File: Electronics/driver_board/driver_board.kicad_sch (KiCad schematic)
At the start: 22 parts, among them J1 Conn_ST_STDC14, J2 Conn_01x02, Q1 IAUZ40N10S5N130, Q2 IAUZ40N10S5N130, Q3 IAUZ40N10S5N130, Q4 IAUZ40N10S5N130, U1 INA241A2xDDF, U2 STM32G491CCT6, U3 REF3433TIDBVR, U4 UCC27302ADRCR, U5 UCC27302ADRCR, U6 LMW78_12-0.5R

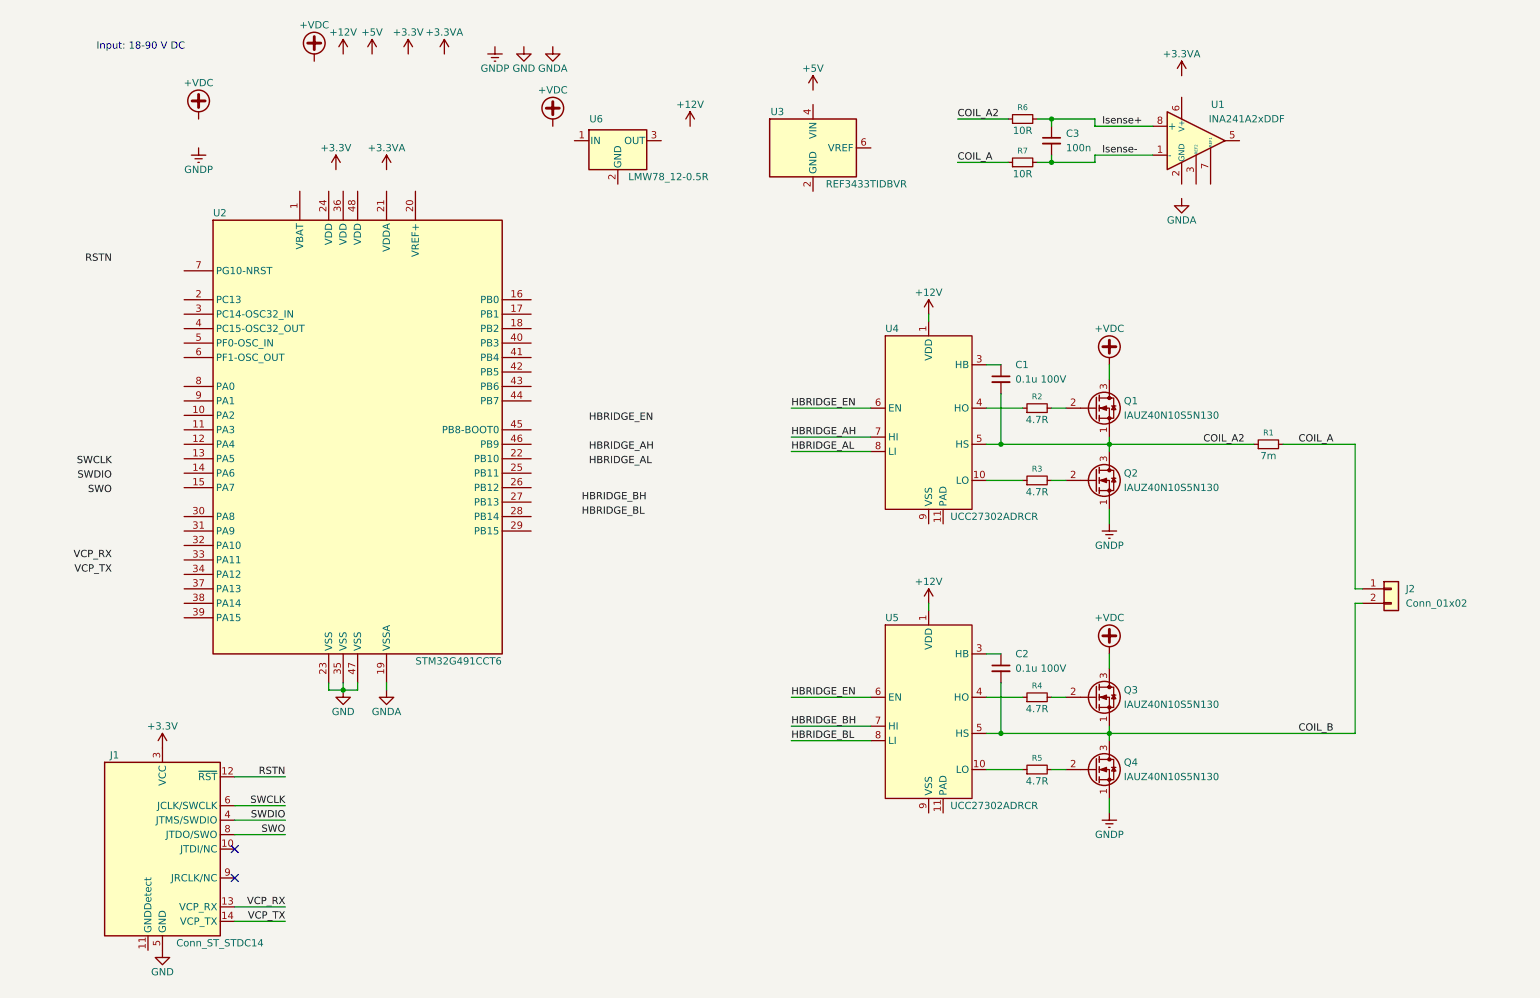
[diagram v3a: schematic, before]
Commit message: [pcb] Added more power supply parts, split power to separate sheet
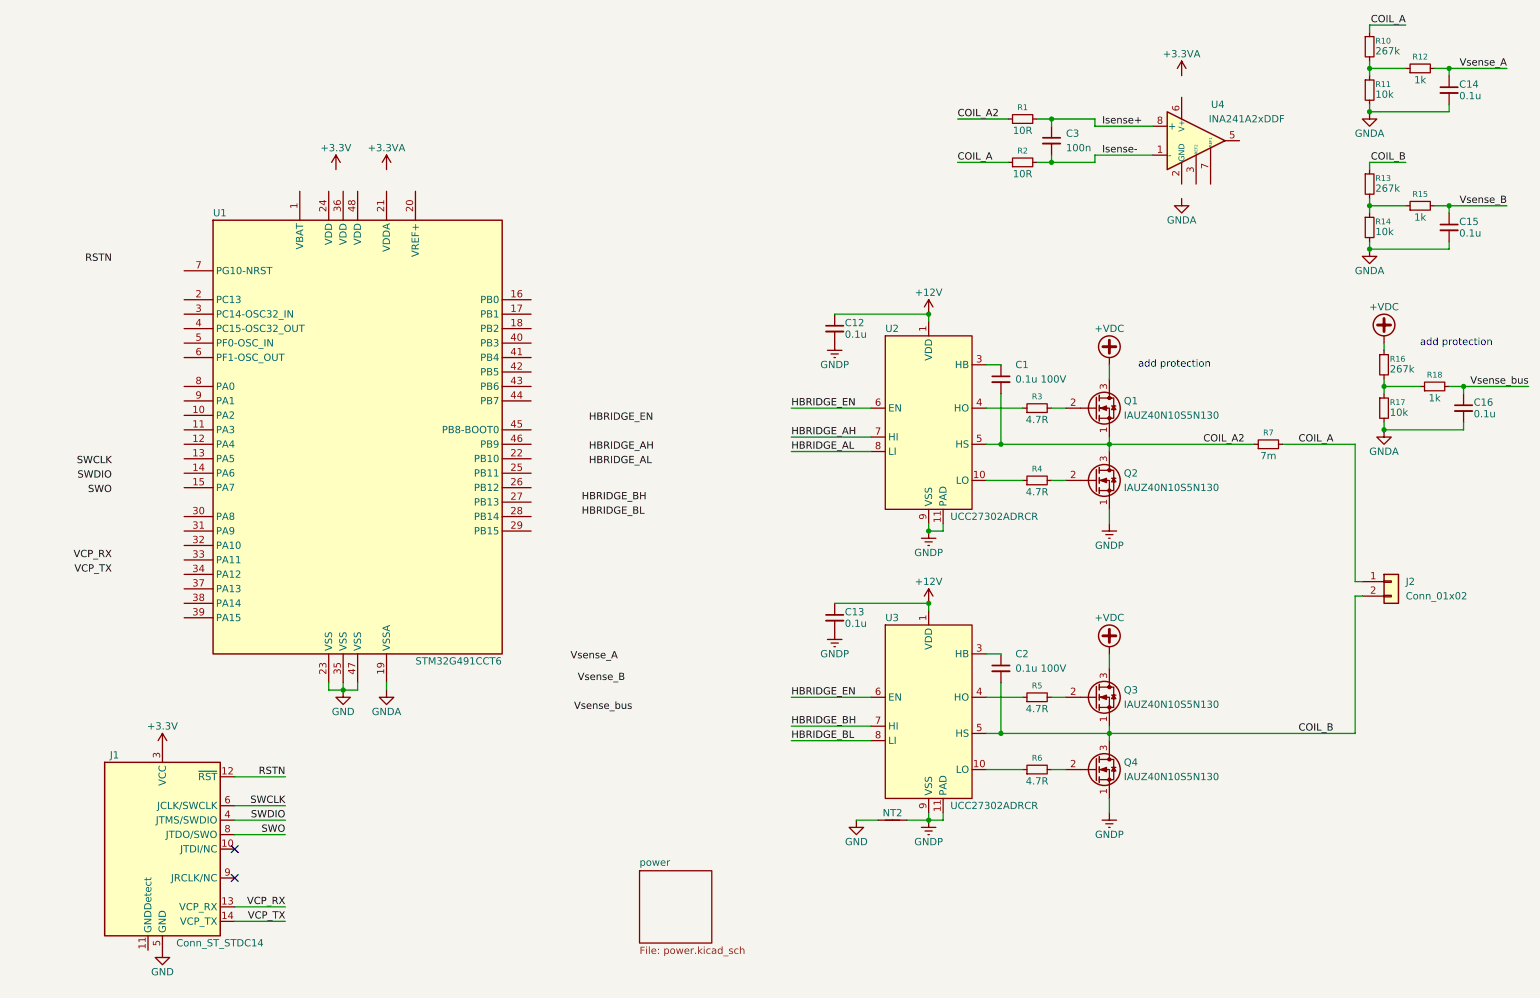
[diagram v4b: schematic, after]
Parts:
- removed U3: REF3433TIDBVR, Package_TO_SOT_SMD:SOT-23-6, symbol DWlib:REF3433TIDBVR
- removed U6: LMW78_12-0.5R, DWlib:Converter_DCDC_GAPTEC_LMW78_THT, symbol DWlib:LMW78_0.5R
- added C12, C13, C14, C15, C16: 0.1u, symbol Device:C_Small
- added NT2: NetTie_2, NetTie:NetTie-2_SMD_Pad0.5mm, symbol Device:NetTie_2
- added R10, R13, R16: 267k, symbol Device:R_Small
- added R11, R14, R17: 10k, symbol Device:R_Small
- added R12, R15, R18: 1k, symbol Device:R_Small
- renumbered R6 to R1, R7 to R2, R2 to R3, R3 to R4, R4 to R5, R5 to R6, R1 to R7, U2 to U1, U4 to U2, U5 to U3, U1 to U4
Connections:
- net +12V: now also C12.1, C13.1
- net +VDC: now also R16.1
- net COIL_A: now also R10.1
- net COIL_B: now also R13.1
- net GND: now also NT2.1
- net GNDA: now also C14.2, C15.2, C16.2, R11.2, R14.2, R17.2
- net GNDP: now also U2.11 (PAD), U2.9 (VSS), U3.11 (PAD), U3.9 (VSS), C12.2, C13.2, NT2.2
- new net: R16.2, R17.1, R18.1
- new net: R13.2, R14.1, R15.1
- new net: R10.2, R11.1, R12.1
- new net Vsense_A: C14.1, R12.2
- new net Vsense_B: C15.1, R15.2
- new net Vsense_bus: C16.1, R18.2
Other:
- added sheet power (power.kicad_sch)
- note added: "add protection"
- note removed: "Input: 18-90 V DC"
- moved on the sheet: J2

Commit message: [pcb] Separated H-bridge to new sheet
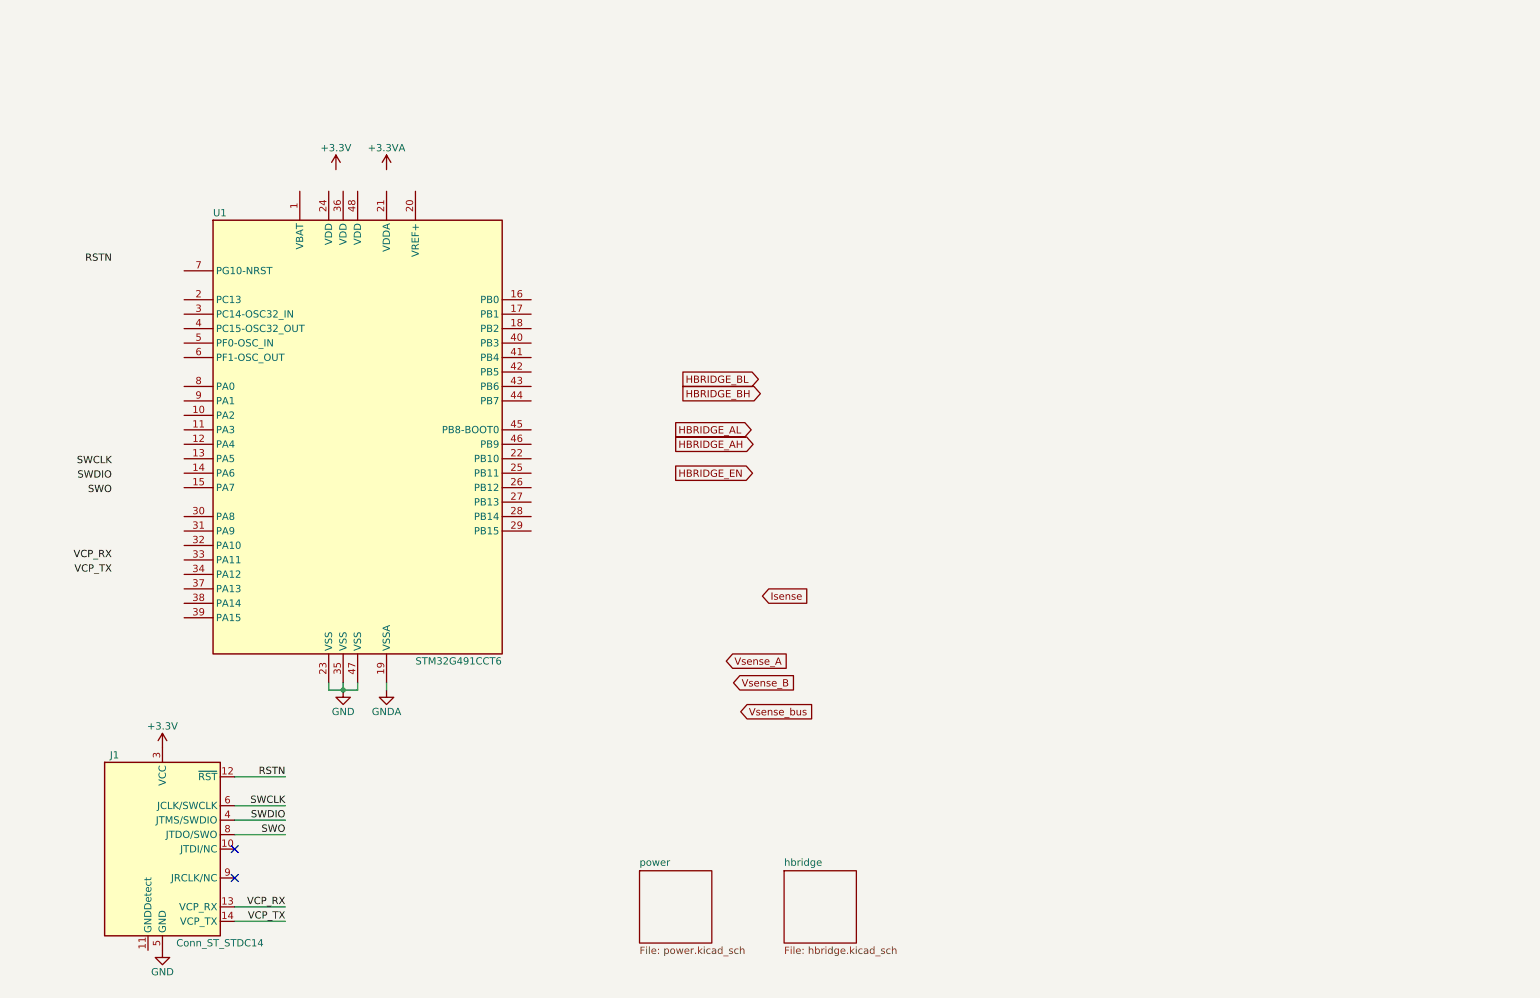
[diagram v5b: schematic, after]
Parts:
- removed C1, C2: 0.1u 100V, symbol Device:C_Small
- removed C12, C13, C14, C15, C16: 0.1u, symbol Device:C_Small
- removed C3: 100n, symbol Device:C_Small
- removed J2: Conn_01x02, symbol Connector_Generic:Conn_01x02
- removed NT2: NetTie_2, NetTie:NetTie-2_SMD_Pad0.5mm, symbol Device:NetTie_2
- removed Q1, Q2, Q3, Q4: IAUZ40N10S5N130, DWlib:Infineon_PG-TSDSON-8-33, symbol DWlib:IAUZ40N10S5N130
- removed R1, R2: 10R, symbol Device:R_Small
- removed R10, R13, R16: 267k, symbol Device:R_Small
- removed R11, R14, R17: 10k, symbol Device:R_Small
- removed R12, R15, R18: 1k, symbol Device:R_Small
- removed R3, R4, R5, R6: 4.7R, symbol Device:R_Small
- removed R7: 7m, Resistor_SMD:R_2512_6332Metric, symbol Device:R_Small
- removed U2, U3: UCC27302ADRCR, DWlib:TI_VSON-10-1EP_3x3mm_P0.5mm_EP1.65x2.4mm, symbol DWlib:UCC27302ADRCR
- removed U4: INA241A2xDDF, Package_TO_SOT_SMD:SOT-23-8, symbol Amplifier_Current:INA241A2xDDF
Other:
- added sheet hbridge (hbridge.kicad_sch)
- note removed: "add protection"

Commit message: [pcb] Added regulators, pin mapping
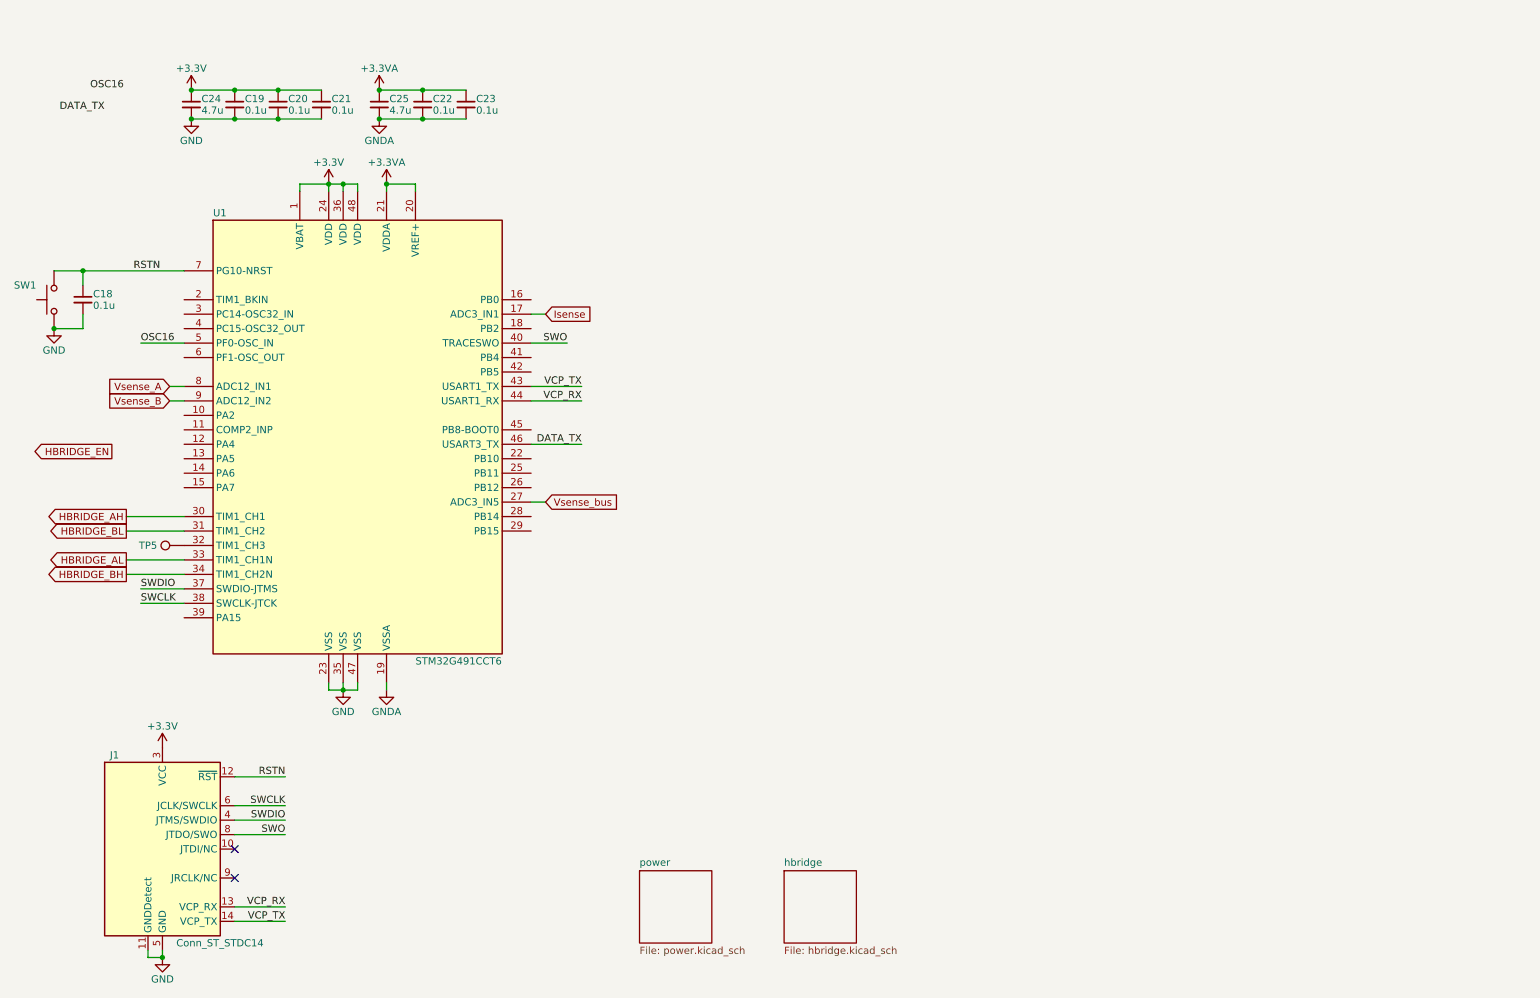
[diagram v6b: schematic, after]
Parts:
- added C18, C19, C20, C21, C22, C23: 0.1u, symbol Device:C_Small
- added C24, C25: 4.7u, symbol Device:C_Small
- added SW1: TL3305, DWlib:SW_Push_1P1T_NO_E-Switch_TL3305AFxxxQG, symbol Switch:SW_Push
- added TP5: TestPoint, Connector_PinHeader_1.00mm:PinHeader_1x01_P1.00mm_Vertical, symbol Connector:TestPoint
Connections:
- net +3.3V: now also U1.1 (VBAT), U1.24 (VDD), U1.36 (VDD), U1.48 (VDD), C19.1, C20.1, C21.1, C24.1
- net +3.3VA: now also U1.20 (VREF+), U1.21 (VDDA), C22.1, C23.1, C25.1
- net GND: now also J1.11 (GNDDetect), C18.2, C19.2, C20.2, C21.2, C24.2, SW1.1
- net GNDA: now also C22.2, C23.2, C25.2
- net HBRIDGE_AH: now also U1.30 (PA8)
- net HBRIDGE_AL: now also U1.33 (PA11)
- net HBRIDGE_BH: now also U1.34 (PA12)
- net HBRIDGE_BL: now also U1.31 (PA9)
- net Isense: now also U1.17 (PB1)
- net RSTN: now also U1.7 (PG10-NRST), C18.1, SW1.2
- net SWCLK: now also U1.38 (PA14)
- net SWDIO: now also U1.37 (PA13)
- net SWO: now also U1.40 (PB3)
- net VCP_RX: now also U1.44 (PB7)
- net VCP_TX: now also U1.43 (PB6)
- net Vsense_A: now also U1.8 (PA0)
- net Vsense_B: now also U1.9 (PA1)
- net Vsense_bus: now also U1.27 (PB13)
- net at U1.32 (PA10): now also TP5.1
- net DATA_TX: now reaches U1.46 (PB9)
- net OSC16: now reaches U1.5 (PF0-OSC_IN)
